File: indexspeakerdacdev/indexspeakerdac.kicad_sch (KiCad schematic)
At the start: 41 parts, among them IC1 MAX98360AEFB+T, IC2 MAX98360AEFB+T, IC3 W25Q16JVUXIQ_TR, J1 Conn_01x04_Pin, J2 Conn_01x11_Pin, J3 Conn_01x01_Pin, J4 Conn_01x11_Pin, J5 Conn_01x01_Pin, J6 USB_C_Plug_USB2.0, U1 RP2040, U2 MIC5317-3.3xM5, Y1 Crystal_GND24

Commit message: Add files via upload
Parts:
- removed J6: USB_C_Plug_USB2.0, nrfmicro:USB-C-C168688, symbol Connector:USB_C_Plug_USB2.0
- added J6: USB_C_Receptacle_USB2.0, symbol Connector:USB_C_Receptacle_USB2.0
- added R6: 5.1K, Resistor_SMD:R_0201_0603Metric, symbol Device:R
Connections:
- net D+: now also J6.A6 (D+), J6.B6 (D+)
- net D-: now also J6.A7 (D-), J6.B7 (D-)
- net GND: now also J6.A1 (GND), J6.A12 (GND), J6.B1 (GND), J6.B12 (GND), R6.2
- net VCC: now also J6.A4 (VBUS), J6.A9 (VBUS), J6.B4 (VBUS), J6.B9 (VBUS)
- net at R5.1: now also J6.A5 (CC1)
- new net: J6.B5 (CC2), R6.1

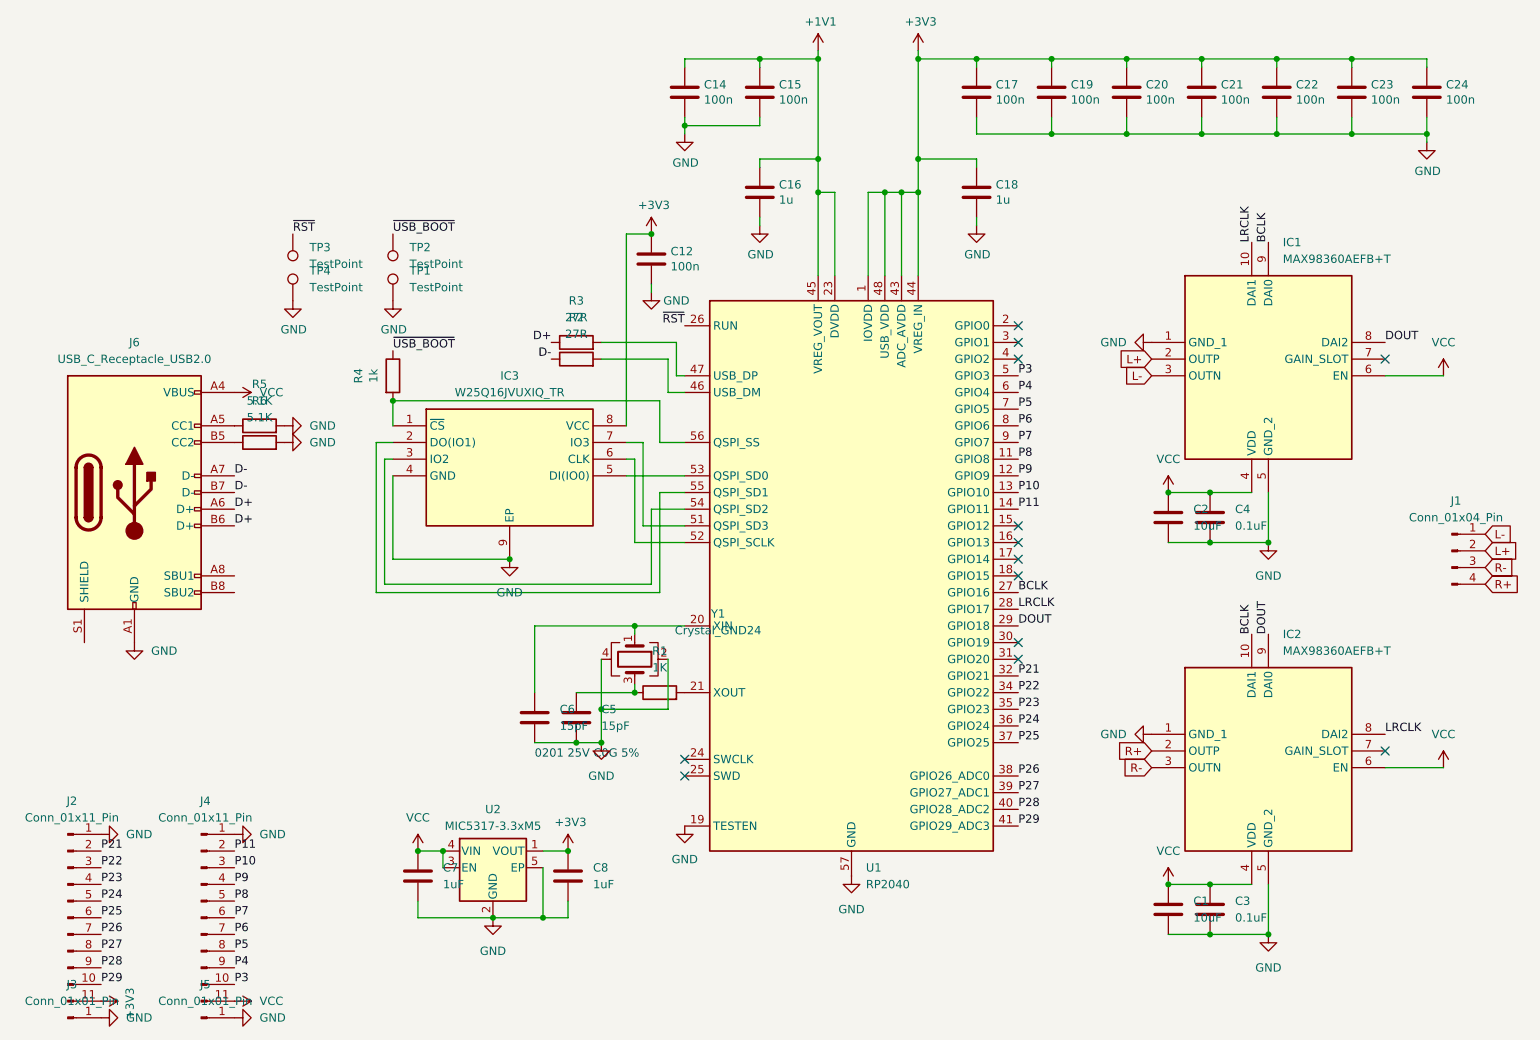
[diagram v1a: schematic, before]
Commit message: Add bom
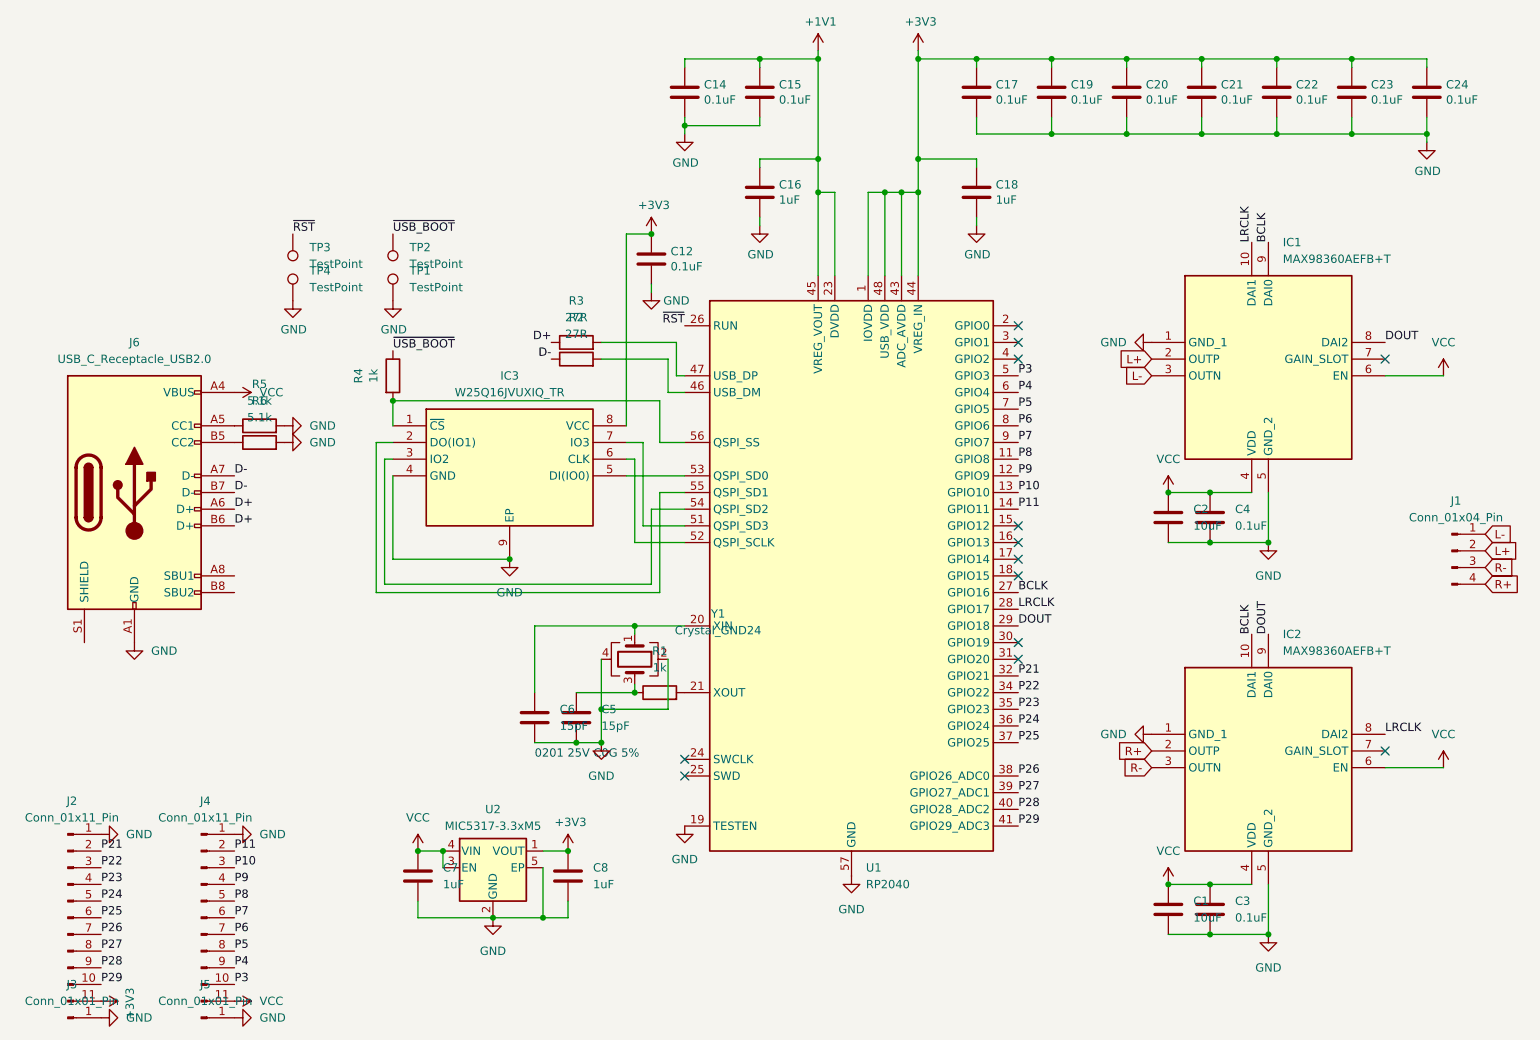
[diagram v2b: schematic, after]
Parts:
- C1, C2: Manufacturer_Name (none) -> Murata; Manufacturer_Part_Number (none) -> GRM188C81A106MA73D; Mouser Part Number (none) -> 81-GRM188C81A106MA3D
- C12, C14, C15, C17, C19, C20, C21, C22, C23, C24: value 100n -> 0.1uF; Manufacturer_Name (none) -> Murata; Manufacturer_Part_Number (none) -> GRM033C80J104KE15D; Mouser Part Number (none) -> 81-GRM33C80J104KE15D
- C16, C18: value 1u -> 1uF; Manufacturer_Name (none) -> Murata; Manufacturer_Part_Number (none) -> GRM155C81A105KA12J; Mouser Part Number (none) -> 81-GRM155C81A105KA2J
- C3, C4: Manufacturer_Name (none) -> Murata; Manufacturer_Part_Number (none) -> GRM155R61A104KA01J; Mouser Part Number (none) -> 81-GRM15R61A104KA01J
- C5, C6: Manufacturer_Name (none) -> Murata; Manufacturer_Part_Number (none) -> GRM0335C1E150JA01D; Mouser Part Number (none) -> 81-GRM0335C1E150JA1D
- C7, C8: Manufacturer_Name (none) -> Murata; Manufacturer_Part_Number (none) -> GRM155C81A105KA12J; Mouser Part Number (none) -> 81-GRM155C81A105KA2J
- IC1, IC2: Manufacturer_Name Analog Devices -> Analog Devices Inc.; Mouser Price/Stock https://www.mouser.co.uk/ProductDetail/Maxim-Integrated/MAX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 -> (none)
- IC3: Height 0.6 -> (none); Mouser Price/Stock https://www.mouser.co.uk/ProductDetail/Winbond/W25Q16JVUXIQ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 -> (none)
- J6: Manufacturer_Name (none) -> Global Connector Technology (GCT); Manufacturer_Part_Number (none) -> USB4510-03-1-A; Mouser Part Number (none) -> 640-USB4510031A
- R1: value 1K -> 1k; Manufacturer_Name (none) -> Vishay; Manufacturer_Part_Number (none) -> CRCW04021K00FKED; Mouser Part Number (none) -> 71-CRCW0402-1.0K-E3
- R2, R3: Manufacturer_Name (none) -> YAGEO; Manufacturer_Part_Number (none) -> RC0201FR-0727RL; Mouser Part Number (none) -> 603-RC0201FR-0727RL
- R4: Manufacturer_Name (none) -> Bourns; Manufacturer_Part_Number (none) -> CR0201-FW-1001GLF; Mouser Part Number (none) -> 652-CR0201FW-1001GLF
- R5, R6: value 5.1K -> 5.1k; Manufacturer_Name (none) -> YAGEO; Manufacturer_Part_Number (none) -> RC0201JR-075K1L; Mouser Part Number (none) -> 603-RC0201JR-075K1L
- U1: Manufacturer_Name (none) -> Raspberry Pi; Manufacturer_Part_Number (none) -> SC0914(7); Mouser Part Number (none) -> 358-SC09147
- U2: Manufacturer_Name (none) -> Microchip; Manufacturer_Part_Number (none) -> MIC5317-3.3YMT-TR; Mouser Part Number (none) -> 494-MIC531733YMTTR
- Y1: Manufacturer_Name (none) -> ECS; Manufacturer_Part_Number (none) -> ECS-120-10-33-AGM-TR; Mouser Part Number (none) -> 520-120-10-33-AGMT
